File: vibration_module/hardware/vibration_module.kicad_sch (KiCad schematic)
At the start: 17 parts, among them J1 I2C/PWR, SW2 SW_SPST, U2 DRV2605LDGS, U3 STM32G031G8Ux, U4 TPS7A20xxxDQN

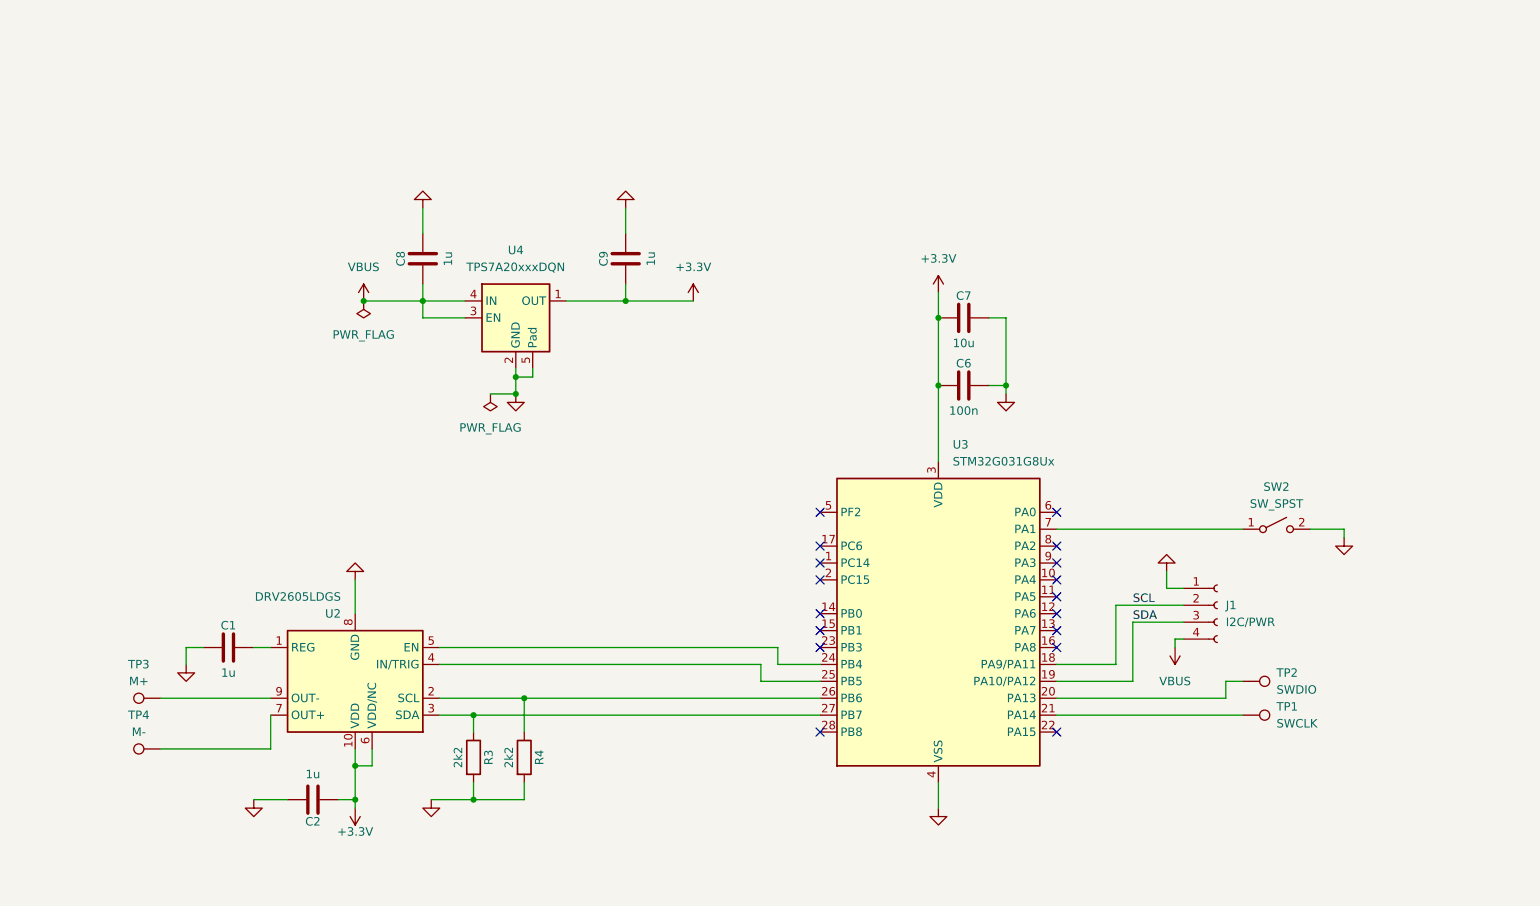
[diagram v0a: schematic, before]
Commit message: update pcb layout, change switch bom
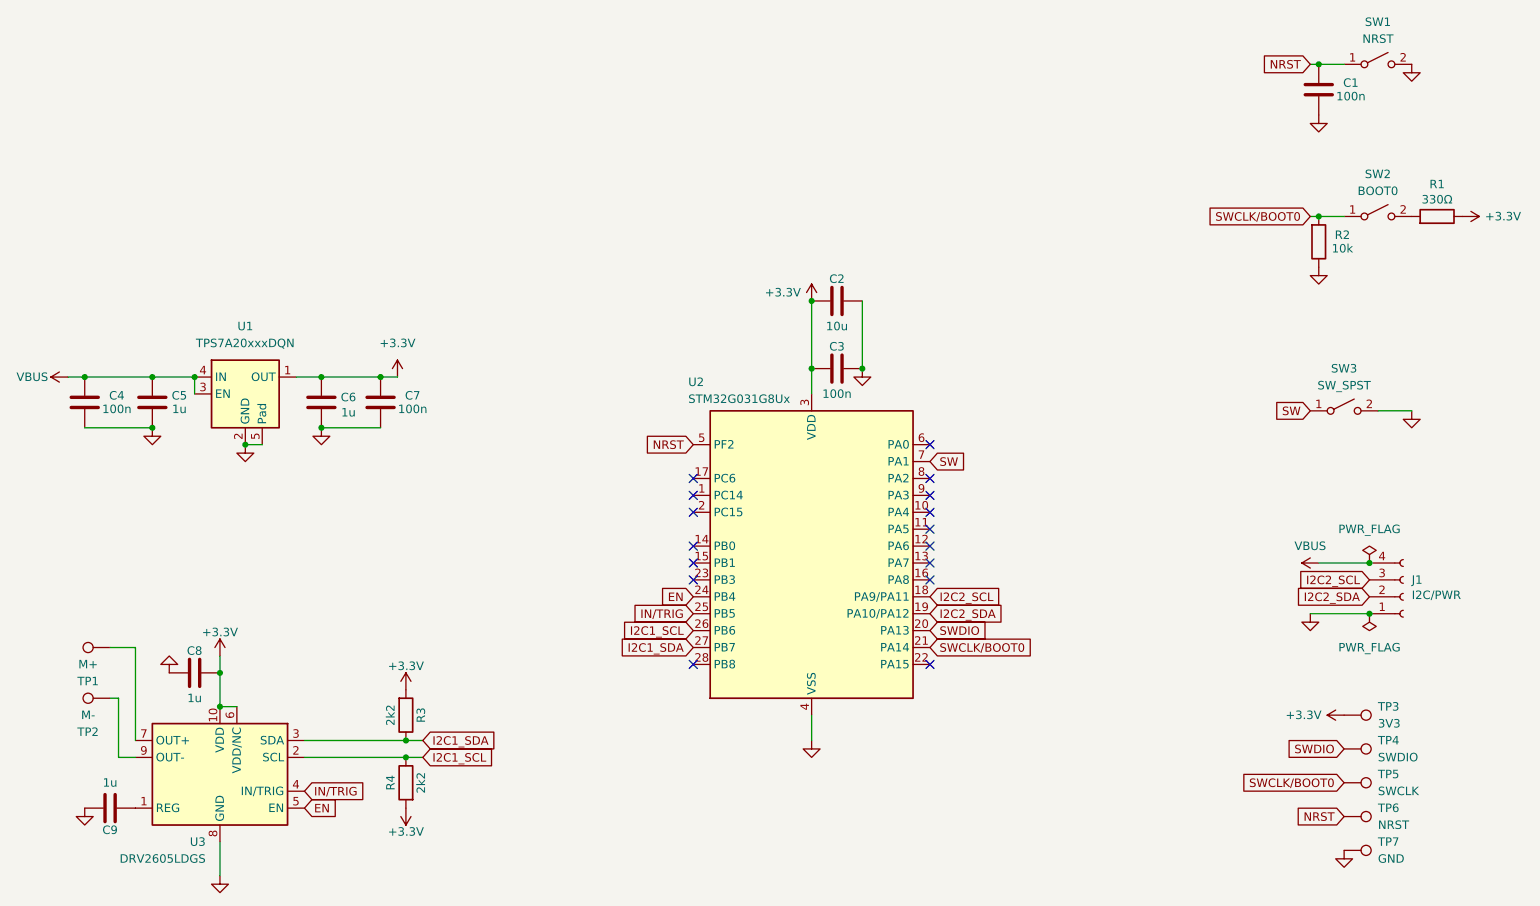
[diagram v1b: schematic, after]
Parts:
- added C1, C4, C7: 100n, Capacitor_SMD:C_0402_1005Metric, symbol Device:C
- added R1: 330Ω, Resistor_SMD:R_0402_1005Metric, symbol Device:R
- added R2: 10k, Resistor_SMD:R_0402_1005Metric, symbol Device:R
- added SW1: NRST, PCM_JLCPCB:SW_TS-1088-AR02016, symbol Switch:SW_SPST
- added SW2: BOOT0, PCM_JLCPCB:SW_TS-1088-AR02016, symbol Switch:SW_SPST
- added TP3: 3V3, TestPoint:TestPoint_Pad_D1.0mm, symbol Connector:TestPoint
- added TP6: NRST, TestPoint:TestPoint_Pad_D1.0mm, symbol Connector:TestPoint
- added TP7: GND, TestPoint:TestPoint_Pad_D1.0mm, symbol Connector:TestPoint
- SW3: renamed from SW2; footprint PCM_Switch_Keyboard_Kailh:SW_Kailh_Choc_V1_1.00u -> PCM_JLCPCB:SW_TS-1088-AR02016
- TP1: renamed from TP4; value M- -> M+
- TP2: renamed from TP3; value M+ -> M-
- TP4: renamed from TP2; footprint TestPoint:TestPoint_THTPad_D1.0mm_Drill0.5mm -> TestPoint:TestPoint_Pad_D1.0mm
- TP5: renamed from TP1; footprint TestPoint:TestPoint_THTPad_D1.0mm_Drill0.5mm -> TestPoint:TestPoint_Pad_D1.0mm
- renumbered C7 to C2, C6 to C3, C8 to C5, C9 to C6, C2 to C8, C1 to C9, U4 to U1, U3 to U2, U2 to U3
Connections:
- net +3.3V: now also C6.2, R3.2, R4.2, C7.2, R1.1, TP3.1; no longer C6.1
- net GND: now also C5.1, C6.1, C1.1, C4.1, C7.1, R2.1, SW1.2 (B), TP7.1; no longer C5.2, C6.2, R3.2, R4.2
- net VBUS: now also C5.2, C4.2; no longer C5.1
- net SWCLK/BOOT0: now reaches TP5.1, U2.21 (PA14)
- net SWCLK/BOOT0: now also R2.2, SW2.1 (A)
- net I2C1_SCL: now reaches R4.1, U2.26 (PB6), U3.2 (SCL)
- net SW: now reaches SW3.1 (A), U2.7 (PA1)
- net SWDIO: now reaches TP4.1, U2.20 (PA13)
- net EN: now reaches U2.24 (PB4), U3.5 (EN)
- net IN/TRIG: now reaches U2.25 (PB5), U3.4 (IN/TRIG)
- net I2C1_SDA: now reaches R3.1, U2.27 (PB7), U3.3 (SDA)
- net NRST: now reaches U2.5 (PF2)
- net NRST: now also C1.2, SW1.1 (A), TP6.1
- net SCL renamed I2C2_SCL
- net I2C2_SCL: now also J1.3 (Pin_3); no longer J1.2 (Pin_2)
- net SDA renamed I2C2_SDA
- net I2C2_SDA: now also J1.2 (Pin_2); no longer J1.3 (Pin_3)
- new net: R1.2, SW2.2 (B)
- no-connect marks 17 -> 16
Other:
- moved on the sheet: C2, C3, C5, C6, C8, C9, J1, R3, R4, SW3, TP1, TP2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
